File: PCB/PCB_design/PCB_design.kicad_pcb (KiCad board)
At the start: 2 copper layers, 17.8 x 11.9 mm, 7 parts, among them J1 Conn_01x02_Pin, U1 NE555D

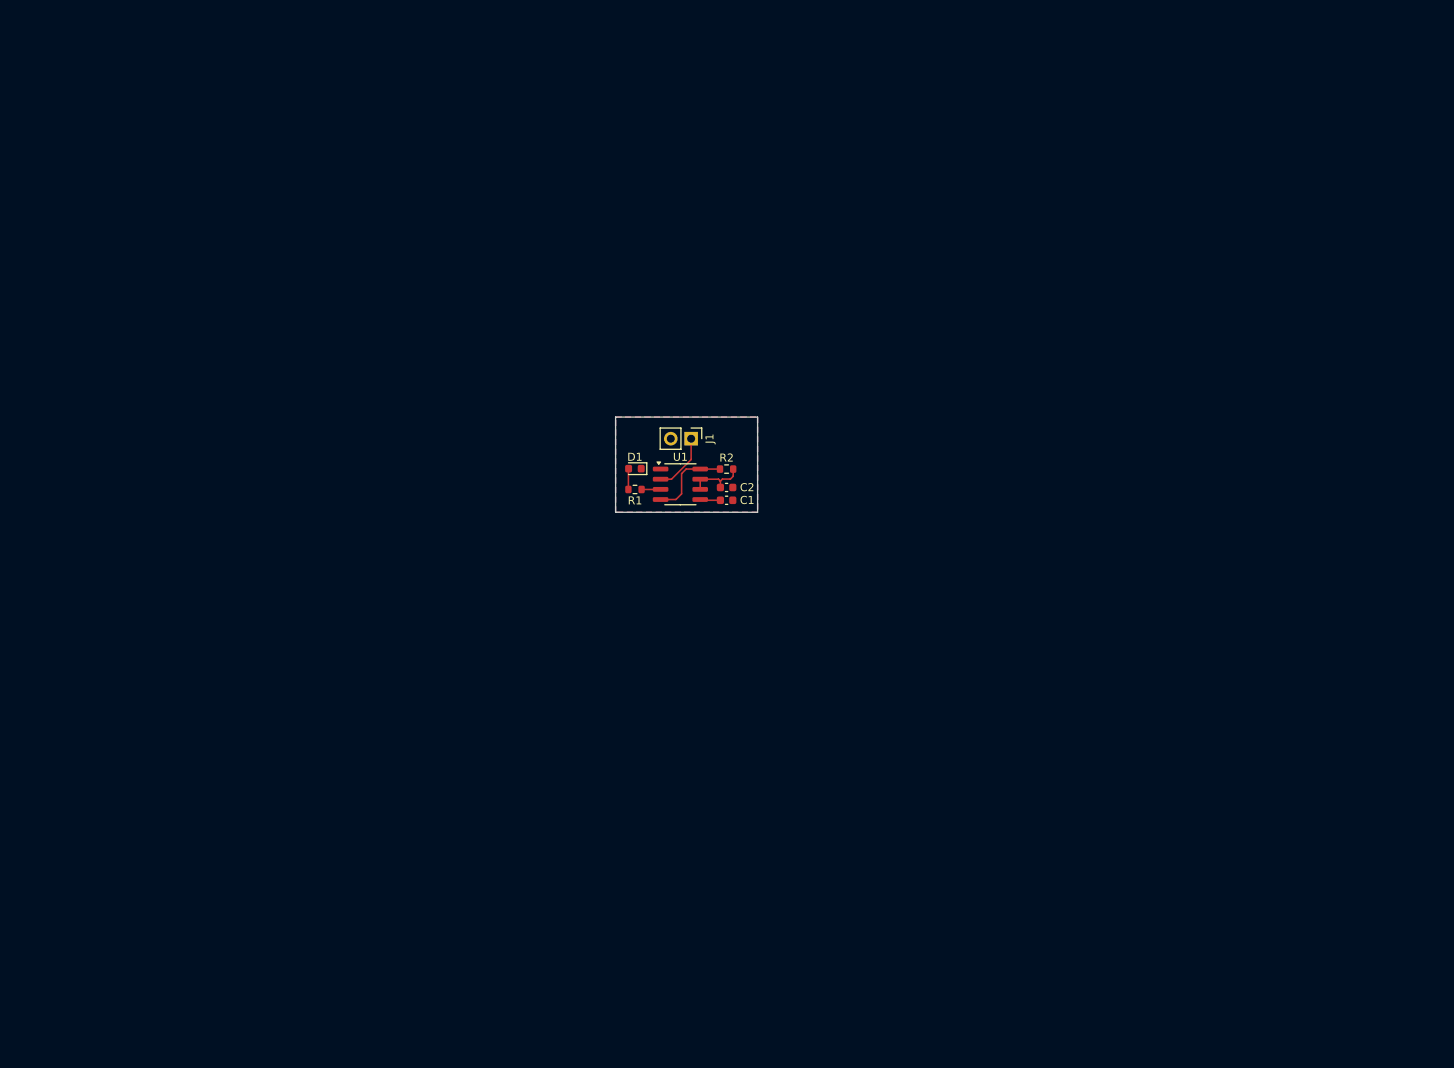
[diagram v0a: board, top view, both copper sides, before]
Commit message: Début routage
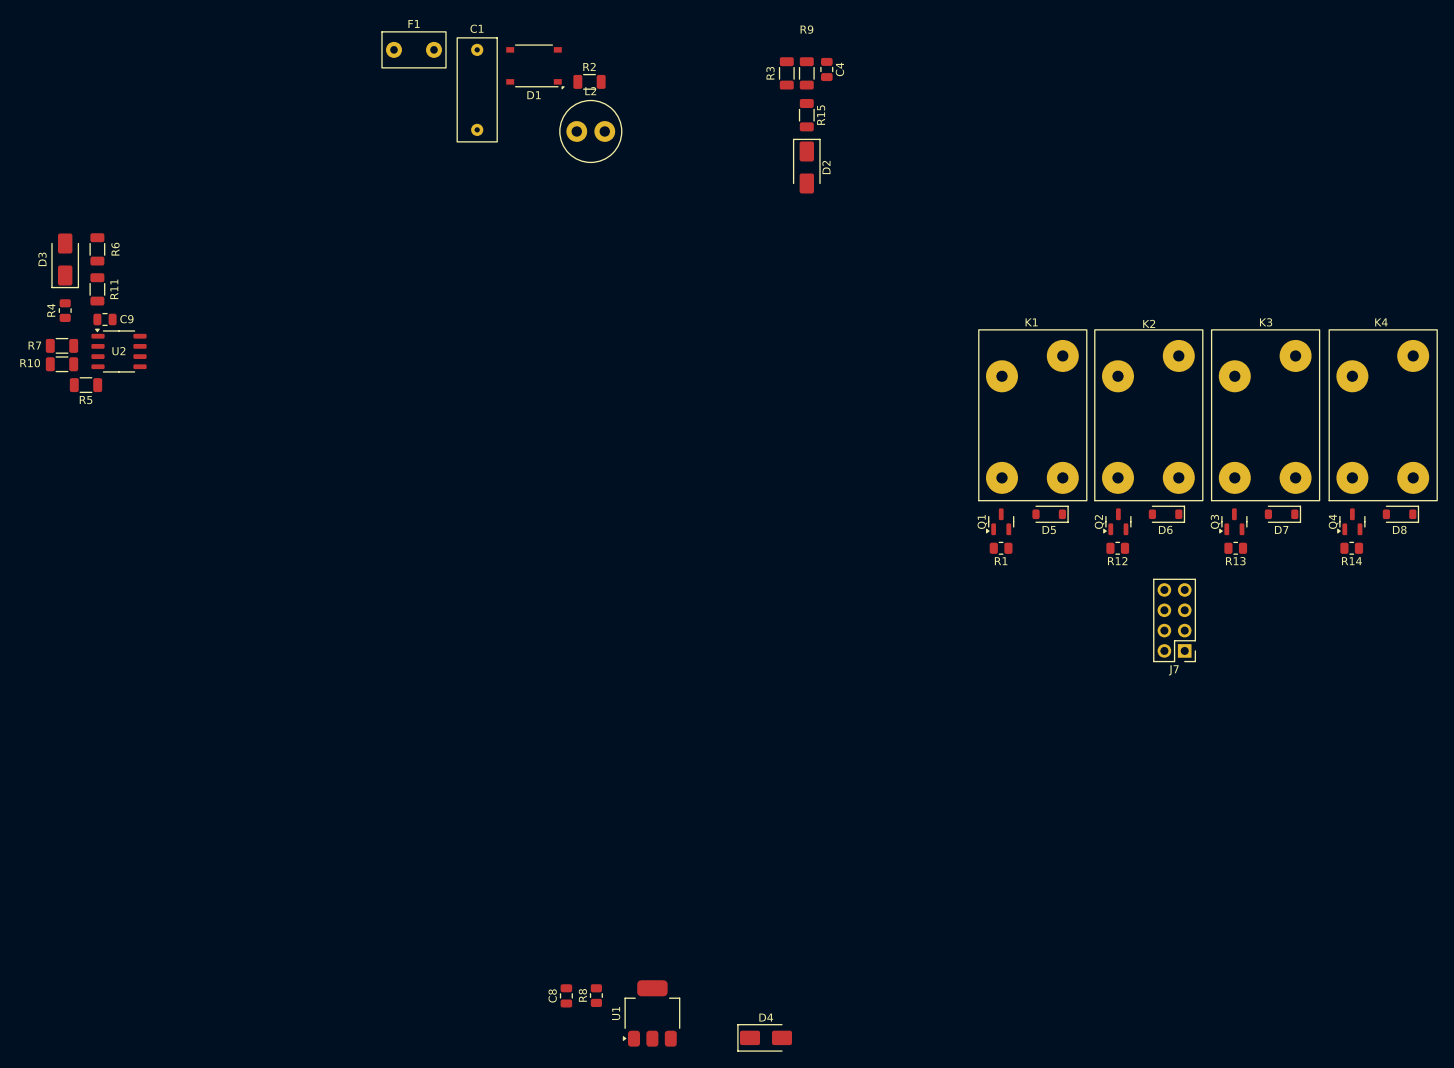
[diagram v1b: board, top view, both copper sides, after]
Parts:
- removed C2: C_Polarized, Capacitor_SMD:C_0603_1608Metric
- removed J1: Conn_01x02_Pin, Connector_PinHeader_2.54mm:PinHeader_1x02_P2.54mm_Vertical
- added C4: 100p/400V, Capacitor_SMD:C_0805_2012Metric, F.Cu at (137.8, 24.6)
- added C8: 0,1u/10V, Capacitor_SMD:C_0805_2012Metric, F.Cu at (105.2, 140.4)
- added C9: 4,7u/25V, Capacitor_SMD:C_0805_2012Metric, F.Cu at (47.6, 55.9)
- added D2: D, Diode_SMD:D_SMA, F.Cu at (135.3, 36.9)
- added D3: D, Diode_SMD:D_SMA, F.Cu at (42.6, 48.4)
- added D4: D, Diode_SMD:D_SMA, F.Cu at (130.2, 145.7)
- added D5: D, Diode_SMD:D_SOD-123, F.Cu at (165.6, 80.2)
- added D6: D, Diode_SMD:D_SOD-123, F.Cu at (180.2, 80.2)
- added D7: D, Diode_SMD:D_SOD-123, F.Cu at (194.7, 80.2)
- added D8: D, Diode_SMD:D_SOD-123, F.Cu at (209.4, 80.2)
- added F1: 68, Touch_Switch_Custom:Fuse, F.Cu at (86.2, 22.2)
- added J7: Conn_02x04_Counter_Clockwise, Connector_PinHeader_2.54mm:PinHeader_2x04_P2.54mm_Vertical, F.Cu at (182.5, 97.3)
- added K1: Relay_SPST-NO, Touch_Switch_Custom:FH17-1A2STLE-DC5V, F.Cu at (167.3, 75.7)
- added K2: Relay_SPST-NO, Touch_Switch_Custom:FH17-1A2STLE-DC5V, F.Cu at (181.8, 75.7)
- added K3: Relay_SPST-NO, Touch_Switch_Custom:FH17-1A2STLE-DC5V, F.Cu at (196.4, 75.7)
- added K4: Relay_SPST-NO, Touch_Switch_Custom:FH17-1A2STLE-DC5V, F.Cu at (211.1, 75.7)
- added L2: 3m, Inductor_THT:L_Radial_D7.5mm_P3.50mm_Fastron_07P, F.Cu at (106.5, 32.4)
- added Q1: MMBT3904, Package_TO_SOT_SMD:SOT-23, F.Cu at (159.6, 81.2)
- added Q2: MMBT3904, Package_TO_SOT_SMD:SOT-23, F.Cu at (174.2, 81.2)
- added Q3: MMBT3904, Package_TO_SOT_SMD:SOT-23, F.Cu at (188.8, 81.2)
- added Q4: MMBT3904, Package_TO_SOT_SMD:SOT-23, F.Cu at (203.5, 81.2)
- added R10: 3,9k, Resistor_SMD:R_1206_3216Metric, F.Cu at (42.2, 61.5)
- added R11: 2M, Resistor_SMD:R_1206_3216Metric, F.Cu at (46.6, 52.1)
- added R12: 10k, Resistor_SMD:R_0805_2012Metric, F.Cu at (174.2, 84.5)
- added R13: 10k, Resistor_SMD:R_0805_2012Metric, F.Cu at (188.9, 84.5)
- added R14: 10k, Resistor_SMD:R_0805_2012Metric, F.Cu at (203.4, 84.5)
- added R15: 100, Resistor_SMD:R_1206_3216Metric, F.Cu at (135.3, 30.4)
- added R3: 430k, Resistor_SMD:R_1206_3216Metric, F.Cu at (132.8, 25.1)
- added R4: 100, Resistor_SMD:R_0805_2012Metric, F.Cu at (42.6, 54.8)
- added R5: 1,5, Resistor_SMD:R_1206_3216Metric, F.Cu at (45.2, 64.1)
- added R6: 2M, Resistor_SMD:R_1206_3216Metric, F.Cu at (46.6, 47.1)
- added R7: 24k, Resistor_SMD:R_1206_3216Metric, F.Cu at (42.2, 59.2)
- added R8: 1k, Resistor_SMD:R_0805_2012Metric, F.Cu at (109.0, 140.4)
- added R9: 430k, Resistor_SMD:R_1206_3216Metric, F.Cu at (135.3, 25.1)
- added U2: ~, Package_SO:SOP-8_3.9x4.9mm_P1.27mm, F.Cu at (49.3, 59.9)
- C1: value C -> 0,1u/400V; footprint Capacitor_SMD:C_0603_1608Metric -> Touch_Switch_Custom:MKP-X2-100NR10
- D1: value LED -> D_Bridge_+-AA; footprint LED_SMD:LED_0603_1608Metric -> Diode_SMD:Diode_Bridge_Diotec_ABS
- R1: value R -> 10k; footprint Resistor_SMD:R_0603_1608Metric -> Resistor_SMD:R_0805_2012Metric
- R2: value R -> 5,6k; footprint Resistor_SMD:R_0603_1608Metric -> Resistor_SMD:R_1206_3216Metric
- U1: value NE555D -> SCJT1117B-3.3-A; footprint Package_SO:SOIC-8_3.9x4.9mm_P1.27mm -> Package_TO_SOT_SMD:SOT-223-3_TabPin2
- moved U1 66.2 mm to (116.0, 142.7), turned to 90 degrees
- moved C1 64.4 mm to (94.1, 22.2), turned to -90 degrees
- moved D1 51.9 mm to (101.2, 24.2)
- moved R2 51.3 mm to (108.1, 26.2), turned to 0 degrees
- moved R1 46.3 mm to (159.6, 84.5)
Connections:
- C1 pad 1: GND -> Net-(C1-Pad1)
- C1 pad 2: Net-(U1-CV) -> N
- D1 pad 1: GND -> Net-(D1-+)
- D1 pad 2: Net-(D1-A) -> GND
- R1 pad 1: Net-(U1-Q) -> GND2
- R1 pad 2: Net-(D1-A) -> CT1
- R2 pad 1: Net-(U1-DIS) -> Net-(D1-+)
- R2 pad 2: VCC -> +310VDC
- U1 pad 1: GND -> GND2
- U1 pad 2: Net-(J1-Pin_1) -> +3.3V
- U1 pad 3: Net-(U1-Q) -> +5VDC
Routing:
- net VCC: track 10.5 -> 0.00 mm
- net Net-(J1-Pin_1): track 7.44 -> 0.00 mm
- net Net-(U1-DIS): track 7.44 -> 0.00 mm
- net Net-(D1-A): track 2.61 -> 0.00 mm
- net Net-(U1-CV): track 2.56 -> 0.00 mm
- net Net-(U1-Q): track 2.38 -> 0.00 mm
- removed copper zone on B.Cu, net GND
- removed copper zone on F.Cu, net GND
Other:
- board outline removed

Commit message: Routage : regroupement des blocs
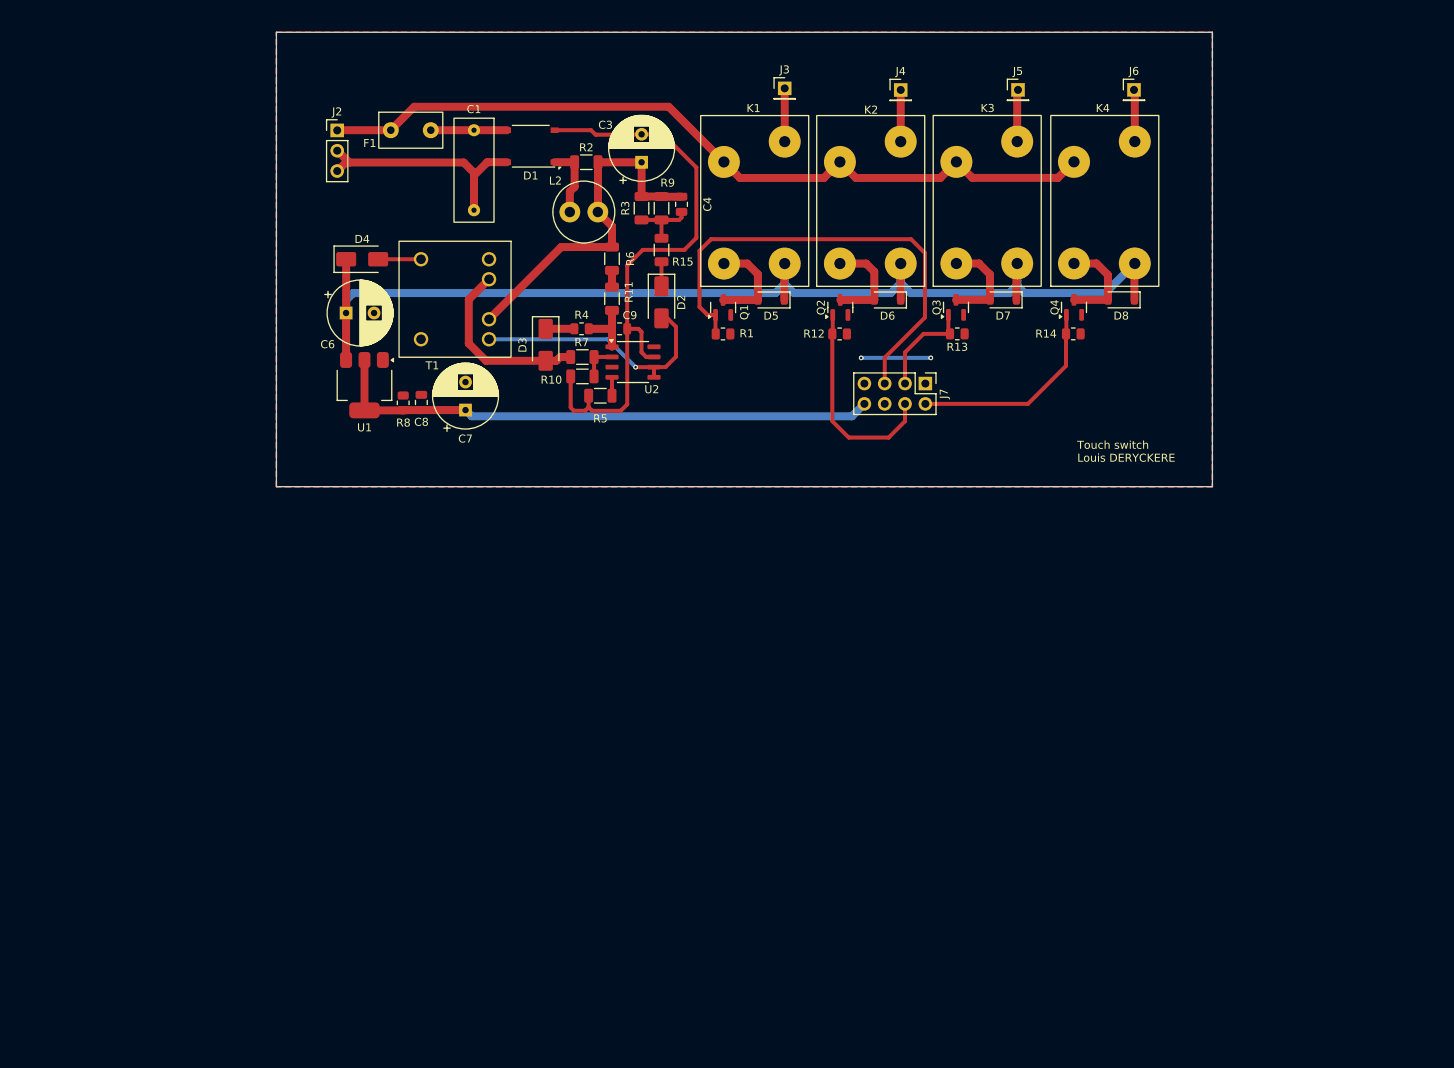
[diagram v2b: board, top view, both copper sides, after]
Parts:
- added C3: 2,2u/400V, Capacitor_THT:CP_Radial_D8.0mm_P3.50mm, F.Cu at (114.7, 36.3)
- added C6: 470u/10V, Capacitor_THT:CP_Radial_D8.0mm_P3.50mm, F.Cu at (77.7, 55.1)
- added C7: 330u/10V, Capacitor_THT:CP_Radial_D8.0mm_P3.50mm, F.Cu at (92.6, 67.2)
- added J2: Conn_01x03_Pin, Connector_PinHeader_2.54mm:PinHeader_1x03_P2.54mm_Vertical, F.Cu at (76.6, 32.3)
- added J3: Conn_01x01_Pin, Connector_PinHeader_2.54mm:PinHeader_1x01_P2.54mm_Vertical, F.Cu at (132.5, 27.0)
- added J4: Conn_01x01_Pin, Connector_PinHeader_2.54mm:PinHeader_1x01_P2.54mm_Vertical, F.Cu at (147.0, 27.2)
- added J5: Conn_01x01_Pin, Connector_PinHeader_2.54mm:PinHeader_1x01_P2.54mm_Vertical, F.Cu at (161.7, 27.2)
- added J6: Conn_01x01_Pin, Connector_PinHeader_2.54mm:PinHeader_1x01_P2.54mm_Vertical, F.Cu at (176.2, 27.2)
- added T1: Transformer_1P_2S, Touch_Switch_Custom:Transformer_V2, F.Cu at (87.1, 48.4)
- moved D4 109.6 mm to (79.7, 48.4)
- moved U1 86.4 mm to (80.0, 64.1), turned to -90 degrees
- moved R8 77.9 mm to (84.8, 66.3), turned to -90 degrees
- moved C8 76.4 mm to (87.1, 66.3), turned to -90 degrees
- moved R10 65.1 mm to (107.2, 63.0)
- moved R7 65.1 mm to (107.2, 60.6)
- moved R4 64.6 mm to (107.1, 57.1), turned to 180 degrees
- moved C9 64.3 mm to (111.9, 57.1)
- moved R11 64.3 mm to (111.0, 53.3)
- moved R6 64.3 mm to (111.0, 48.3)
- moved R5 64.3 mm to (109.5, 65.4)
- moved U2 64.3 mm to (113.6, 61.2)
- moved D3 61.0 mm to (102.7, 59.1), turned to -90 degrees
- moved J7 46.6 mm to (150.1, 63.9), turned to -90 degrees
- moved D7 43.9 mm to (159.8, 53.5)
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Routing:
- net +5VDC: track 0.00 -> 146.6 mm
- net L: track 0.00 -> 101.2 mm
- net GND: track 0.00 -> 75.5 mm
- net +3.3V: track 0.00 -> 69.8 mm
- net CT1: track 0.00 -> 59.7 mm
- net +310VDC: track 0.00 -> 45.2 mm
- net C: track 0.00 -> 32.6 mm, vias 0 -> 1
- net N: track 0.00 -> 30.3 mm
- net CT2: track 0.00 -> 26.2 mm
- net CT4: track 0.00 -> 25.9 mm
- net Vaux: track 0.00 -> 22.9 mm
- net CT3: track 0.00 -> 12.9 mm
- net Net-(D6-A): track 0.00 -> 12.5 mm
- net Net-(D5-A): track 0.00 -> 12.4 mm
- net Net-(D8-A): track 0.00 -> 12.2 mm
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- added copper zone on B.Cu, net GND
- added copper zone on F.Cu, net GND
- added copper zone on F.Cu, net GND2
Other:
- board outline added: 117 x 56.8 mm
- board text added: "Touch switch Louis DERYCKERE"

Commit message: Routage compact
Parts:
- removed U2: ~, Package_SO:SOP-8_3.9x4.9mm_P1.27mm
- added U3: ~, Package_SO:SOP-8_3.9x4.9mm_P1.27mm, F.Cu at (113.6, 61.2)
- moved J6 61.7 mm to (155.7, 85.4), turned to -90 degrees
- moved K4 55.9 mm to (134.0, 85.5), turned to 0 degrees
- moved D8 54.4 mm to (129.5, 83.8), turned to 90 degrees
- moved R14 47.8 mm to (125.2, 77.8), turned to 90 degrees
- moved Q4 46.6 mm to (128.5, 77.9), turned to 0 degrees
- moved J5 44.1 mm to (155.7, 70.9), turned to -90 degrees
- moved K3 35.2 mm to (134.0, 70.8), turned to 0 degrees
- moved D7 34.2 mm to (129.5, 69.1), turned to 90 degrees
- moved J7 32.9 mm to (120.2, 77.7)
- moved J4 30.3 mm to (155.7, 56.2), turned to -90 degrees
- moved R13 29.4 mm to (125.2, 63.3), turned to 90 degrees
- moved J3 27.6 mm to (155.9, 41.8), turned to -90 degrees
- moved Q3 26.9 mm to (128.5, 63.2), turned to 0 degrees
- moved R8 23.9 mm to (108.5, 69.7)
- moved C8 23.9 mm to (110.8, 69.7)
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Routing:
- net CT2: track 26.2 -> 118.9 mm, vias 0 -> 1
- net GND: track 75.5 -> 0.00 mm, vias 0 -> 31
- net CT1: track 59.7 -> 104.8 mm, vias 0 -> 1
- net +3.3V: track 69.8 -> 34.3 mm
- net L: track 101.2 -> 125.3 mm
- net CT4: track 25.9 -> 8.75 mm
- net N: track 30.3 -> 15.6 mm
- net Net-(D4-A): track 5.36 -> 18.5 mm
- net CT3: track 12.9 -> 22.8 mm
- net GND2: track 8.70 -> 0.00 mm, vias 2 -> 20
- net +5VDC: track 146.6 -> 140.6 mm
- added copper zone on B.Cu, net GND2
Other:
- board size 117 x 56.8 mm -> 83.5 x 68.2 mm
